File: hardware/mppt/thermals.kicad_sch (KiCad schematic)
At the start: 27 parts, among them J401 Conn_01x04, J402 Conn_01x03, U401 MCP9700Ax-ELT, U402 MCP9700Ax-ELT

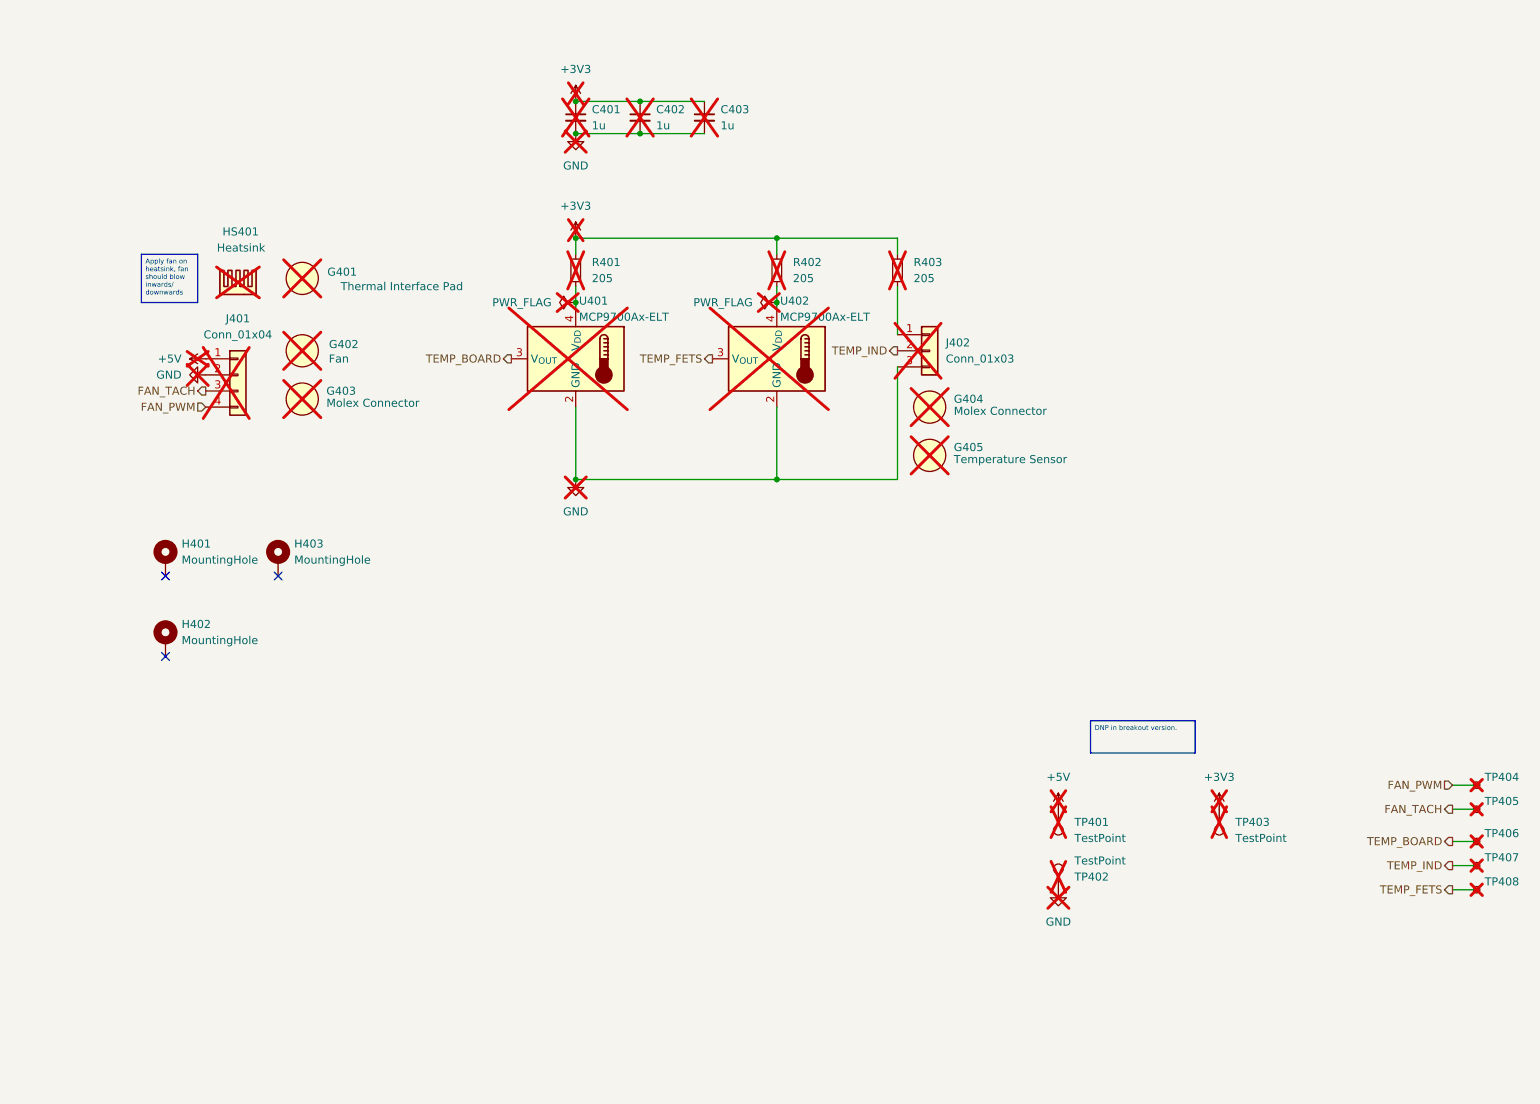
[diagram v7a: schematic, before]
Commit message: unset dnp for all components in sch
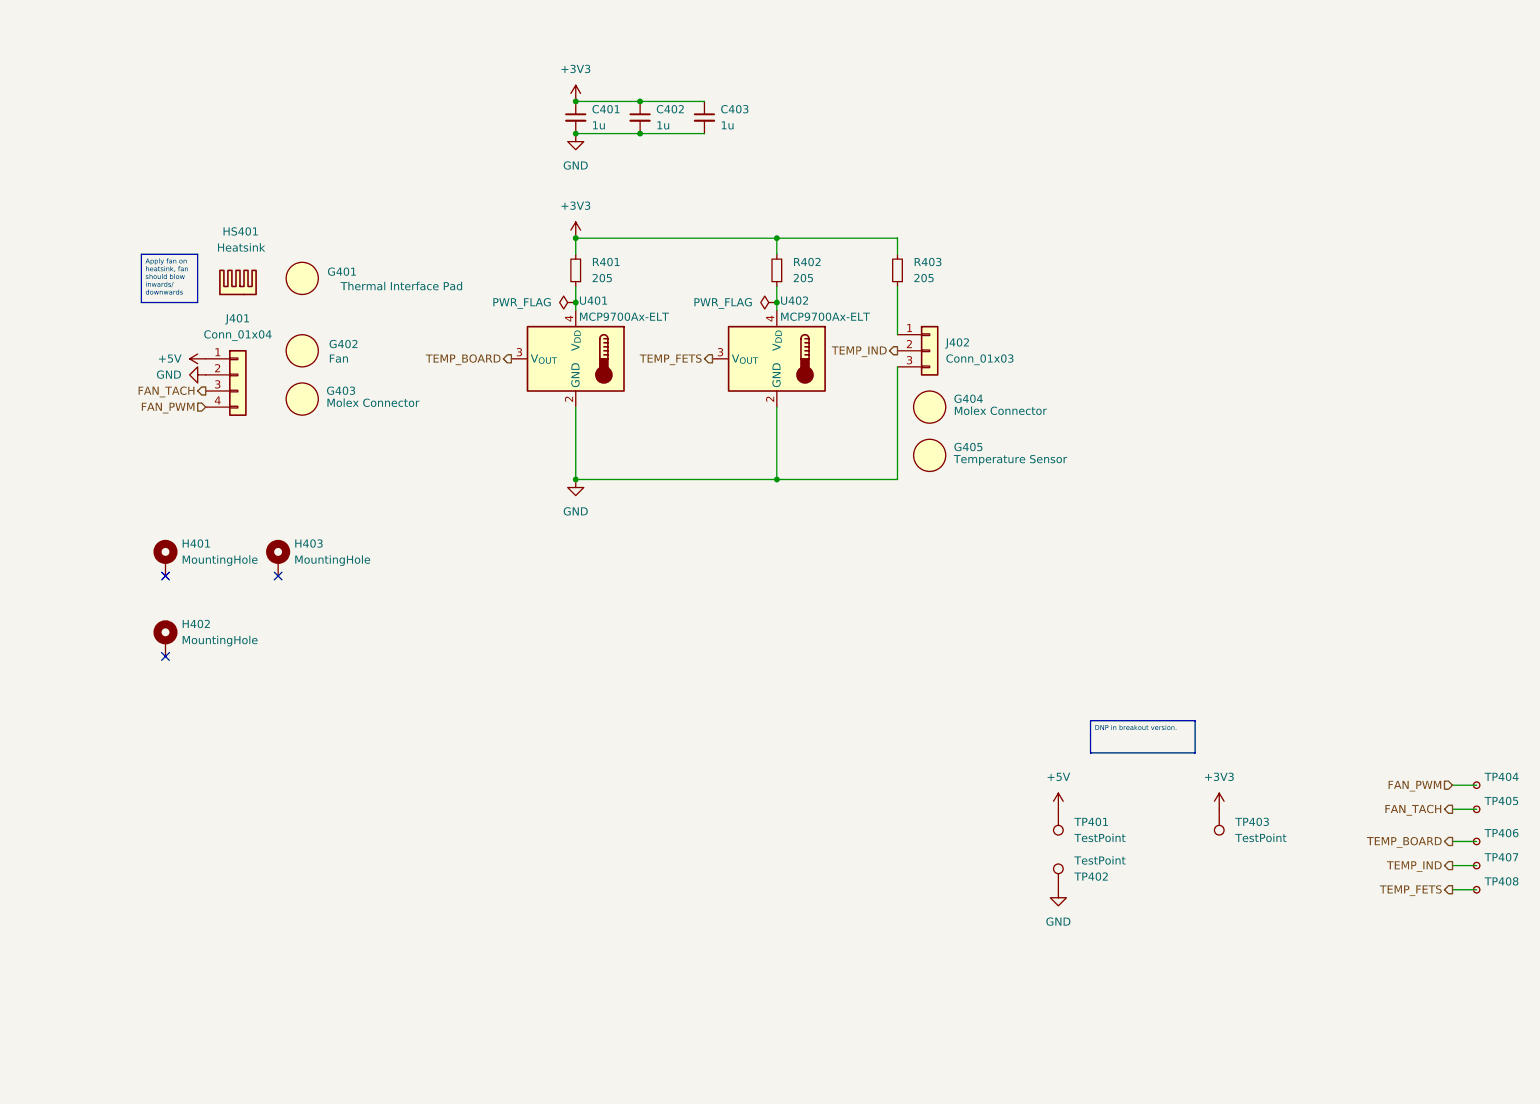
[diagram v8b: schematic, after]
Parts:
- C401, C402, C403, G401, G402, G403, G404, G405, HS401, J401, J402, R401, R402, R403, TP401, TP402, TP403, TP404, TP405, TP406, TP407, TP408, U401, U402: now fitted; now in the parts list
- H401, H402, H403: now in the parts list
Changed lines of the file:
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@@
 		(unit 1)
 		(exclude_from_sim no)
-		(in_bom no)
-		(on_board no)
-		(dnp yes)
+		(in_bom yes)
+		(on_board yes)
+		(dnp no)
 		(fields_autoplaced yes)
 		(property "Reference" "#PWR0407"
@@
 		(unit 1)
 		(exclude_from_sim no)
-		(in_bom no)
-		(on_board no)
-		(dnp yes)
+		(in_bom yes)
+		(on_board yes)
+		(dnp no)
 		(fields_autoplaced yes)
 		(property "Reference" "#PWR0401"
@@
 		(unit 1)
 		(exclude_from_sim no)
-		(in_bom no)
-		(on_board no)
-		(dnp yes)
+		(in_bom yes)
+		(on_board yes)
+		(dnp no)
 		(fields_autoplaced yes)
 		(property "Reference" "#FLG0402"
@@
 		(unit 1)
 		(exclude_from_sim no)
-		(in_bom no)
-		(on_board no)
-		(dnp yes)
+		(in_bom yes)
+		(on_board yes)
+		(dnp no)
 		(fields_autoplaced yes)
 		(property "Reference" "J401"
@@
 		(unit 1)
 		(exclude_from_sim no)
-		(in_bom no)
-		(on_board no)
-		(dnp yes)
+		(in_bom yes)
+		(on_board yes)
+		(dnp no)
 		(property "Reference" "G404"
 			(at 157.48 83.82 0)
@@
 		(unit 1)
 		(exclude_from_sim yes)
-		(in_bom no)
+		(in_bom yes)
 		(on_board yes)
 		(dnp no)
@@
 		(unit 1)
 		(exclude_from_sim no)
-		(in_bom no)
-		(on_board no)
-		(dnp yes)
+		(in_bom yes)
+		(on_board yes)
+		(dnp no)
 		(property "Reference" "G402"
 			(at 63.5 75.184 0)
@@
 		(unit 1)
 		(exclude_from_sim no)
-		(in_bom no)
-		(on_board no)
-		(dnp yes)
+		(in_bom yes)
+		(on_board yes)
+		(dnp no)
 		(fields_autoplaced yes)
 		(property "Reference" "TP405"
@@
 		(unit 1)
 		(exclude_from_sim no)
-		(in_bom no)
-		(on_board no)
-		(dnp yes)
+		(in_bom yes)
+		(on_board yes)
+		(dnp no)
 		(fields_autoplaced yes)
 		(property "Reference" "C402"
@@
 		(unit 1)
 		(exclude_from_sim no)
-		(in_bom no)
-		(on_board no)
-		(dnp yes)
+		(in_bom yes)
+		(on_board yes)
+		(dnp no)
 		(fields_autoplaced yes)
 		(property "Reference" "#PWR0408"
@@
 		(unit 1)
 		(exclude_from_sim no)
-		(in_bom no)
-		(on_board no)
-		(dnp yes)
+		(in_bom yes)
+		(on_board yes)
+		(dnp no)
 		(fields_autoplaced yes)
 		(property "Reference" "#PWR0404"
@@
 		(unit 1)
 		(exclude_from_sim no)
-		(in_bom no)
-		(on_board no)
-		(dnp yes)
+		(in_bom yes)
+		(on_board yes)
+		(dnp no)
 		(fields_autoplaced yes)
 		(property "Reference" "#PWR0406"
@@
 		(unit 1)
 		(exclude_from_sim no)
-		(in_bom no)
-		(on_board no)
-		(dnp yes)
+		(in_bom yes)
+		(on_board yes)
+		(dnp no)
 		(property "Reference" "TP402"
 			(at 176.53 159.2581 0)
@@
 		(unit 1)
 		(exclude_from_sim no)
-		(in_bom no)
-		(on_board no)
-		(dnp yes)
+		(in_bom yes)
+		(on_board yes)
+		(dnp no)
 		(fields_autoplaced yes)
 		(property "Reference" "#PWR0403"
@@
 		(unit 1)
 		(exclude_from_sim no)
-		(in_bom no)
-		(on_board no)
-		(dnp yes)
+		(in_bom yes)
+		(on_board yes)
+		(dnp no)
 		(property "Reference" "HS401"
 			(at 47.752 57.404 0)
@@
 		(unit 1)
 		(exclude_from_sim no)
-		(in_bom no)
-		(on_board no)
-		(dnp yes)
+		(in_bom yes)
+		(on_board yes)
+		(dnp no)
 		(fields_autoplaced yes)
 		(property "Reference" "C401"
@@
 		(unit 1)
 		(exclude_from_sim no)
-		(in_bom no)
-		(on_board no)
-		(dnp yes)
+		(in_bom yes)
+		(on_board yes)
+		(dnp no)
 		(property "Reference" "G405"
 			(at 157.48 91.44 0)
@@
 		(unit 1)
 		(exclude_from_sim no)
-		(in_bom no)
-		(on_board no)
-		(dnp yes)
+		(in_bom yes)
+		(on_board yes)
+		(dnp no)
 		(fields_autoplaced yes)
 		(property "Reference" "TP407"
@@
 		(unit 1)
 		(exclude_from_sim no)
-		(in_bom no)
-		(on_board no)
-		(dnp yes)
+		(in_bom yes)
+		(on_board yes)
+		(dnp no)
 		(fields_autoplaced yes)
 		(property "Reference" "TP403"
@@
 		(unit 1)
 		(exclude_from_sim yes)
-		(in_bom no)
+		(in_bom yes)
 		(on_board yes)
 		(dnp no)
@@
 		(unit 1)
 		(exclude_from_sim no)
-		(in_bom no)
-		(on_board no)
-		(dnp yes)
+		(in_bom yes)
+		(on_board yes)
+		(dnp no)
 		(property "Reference" "U402"
 			(at 130.048 68.326 0)
@@
 		(unit 1)
 		(exclude_from_sim no)
-		(in_bom no)
-		(on_board no)
-		(dnp yes)
+		(in_bom yes)
+		(on_board yes)
+		(dnp no)
 		(fields_autoplaced yes)
 		(property "Reference" "#FLG0401"
@@
 		(unit 1)
 		(exclude_from_sim no)
-		(in_bom no)
-		(on_board no)
-		(dnp yes)
+		(in_bom yes)
+		(on_board yes)
+		(dnp no)
 		(property "Reference" "G401"
 			(at 63.246 63.754 0)
@@
 		(unit 1)
 		(exclude_from_sim no)
-		(in_bom no)
-		(on_board no)
-		(dnp yes)
+		(in_bom yes)
+		(on_board yes)
+		(dnp no)
 		(property "Reference" "G403"
 			(at 58.42 82.55 0)
@@
 		(unit 1)
 		(exclude_from_sim no)
-		(in_bom no)
-		(on_board no)
-		(dnp yes)
+		(in_bom yes)
+		(on_board yes)
+		(dnp no)
 		(fields_autoplaced yes)
 		(property "Reference" "TP404"
@@
 		(unit 1)
 		(exclude_from_sim no)
-		(in_bom no)
-		(on_board no)
-		(dnp yes)
+		(in_bom yes)
+		(on_board yes)
+		(dnp no)
 		(fields_autoplaced yes)
 		(property "Reference" "R401"
@@
 		(unit 1)
 		(exclude_from_sim no)
-		(in_bom no)
-		(on_board no)
-		(dnp yes)
+		(in_bom yes)
+		(on_board yes)
+		(dnp no)
 		(fields_autoplaced yes)
 		(property "Reference" "#PWR0402"
@@
 		(unit 1)
 		(exclude_from_sim no)
-		(in_bom no)
-		(on_board no)
-		(dnp yes)
+		(in_bom yes)
+		(on_board yes)
+		(dnp no)
 		(fields_autoplaced yes)
 		(property "Reference" "TP408"
@@
 		(unit 1)
 		(exclude_from_sim no)
-		(in_bom no)
-		(on_board no)
-		(dnp yes)
+		(in_bom yes)
+		(on_board yes)
+		(dnp no)
 		(property "Reference" "U401"
 			(at 98.298 68.326 0)
@@
 		(unit 1)
 		(exclude_from_sim no)
-		(in_bom no)
-		(on_board no)
-		(dnp yes)
+		(in_bom yes)
+		(on_board yes)
+		(dnp no)
 		(fields_autoplaced yes)
 		(property "Reference" "J402"
@@
 		(unit 1)
 		(exclude_from_sim no)
-		(in_bom no)
-		(on_board no)
-		(dnp yes)
+		(in_bom yes)
+		(on_board yes)
+		(dnp no)
 		(fields_autoplaced yes)
 		(property "Reference" "R402"
@@
 		(unit 1)
 		(exclude_from_sim no)
-		(in_bom no)
-		(on_board no)
-		(dnp yes)
+		(in_bom yes)
+		(on_board yes)
+		(dnp no)
 		(fields_autoplaced yes)
 		(property "Reference" "#PWR0405"
@@
 		(unit 1)
 		(exclude_from_sim no)
-		(in_bom no)
-		(on_board no)
-		(dnp yes)
+		(in_bom yes)
+		(on_board yes)
+		(dnp no)
 		(fields_autoplaced yes)
 		(property "Reference" "#PWR0409"
@@
 		(unit 1)
 		(exclude_from_sim no)
-		(in_bom no)
-		(on_board no)
-		(dnp yes)
+		(in_bom yes)
+		(on_board yes)
+		(dnp no)
 		(fields_autoplaced yes)
 		(property "Reference" "TP401"
@@
 		(unit 1)
 		(exclude_from_sim no)
-		(in_bom no)
-		(on_board no)
-		(dnp yes)
+		(in_bom yes)
+		(on_board yes)
+		(dnp no)
 		(fields_autoplaced yes)
 		(property "Reference" "TP406"
@@
 		(unit 1)
 		(exclude_from_sim no)
-		(in_bom no)
-		(on_board no)
-		(dnp yes)
+		(in_bom yes)
+		(on_board yes)
+		(dnp no)
 		(fields_autoplaced yes)
 		(property "Reference" "R403"
@@
 		(unit 1)
 		(exclude_from_sim yes)
-		(in_bom no)
+		(in_bom yes)
 		(on_board yes)
 		(dnp no)
@@
 		(unit 1)
 		(exclude_from_sim no)
-		(in_bom no)
-		(on_board no)
-		(dnp yes)
+		(in_bom yes)
+		(on_board yes)
+		(dnp no)
 		(fields_autoplaced yes)
 		(property "Reference" "C403"
